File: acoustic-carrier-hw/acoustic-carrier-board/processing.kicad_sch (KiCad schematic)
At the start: 22 parts, among them IC1 ECP5-BGA256, J2 Conn_01x04_Socket, J4 Conn_01x06_Socket, U4 W25Q128JVS

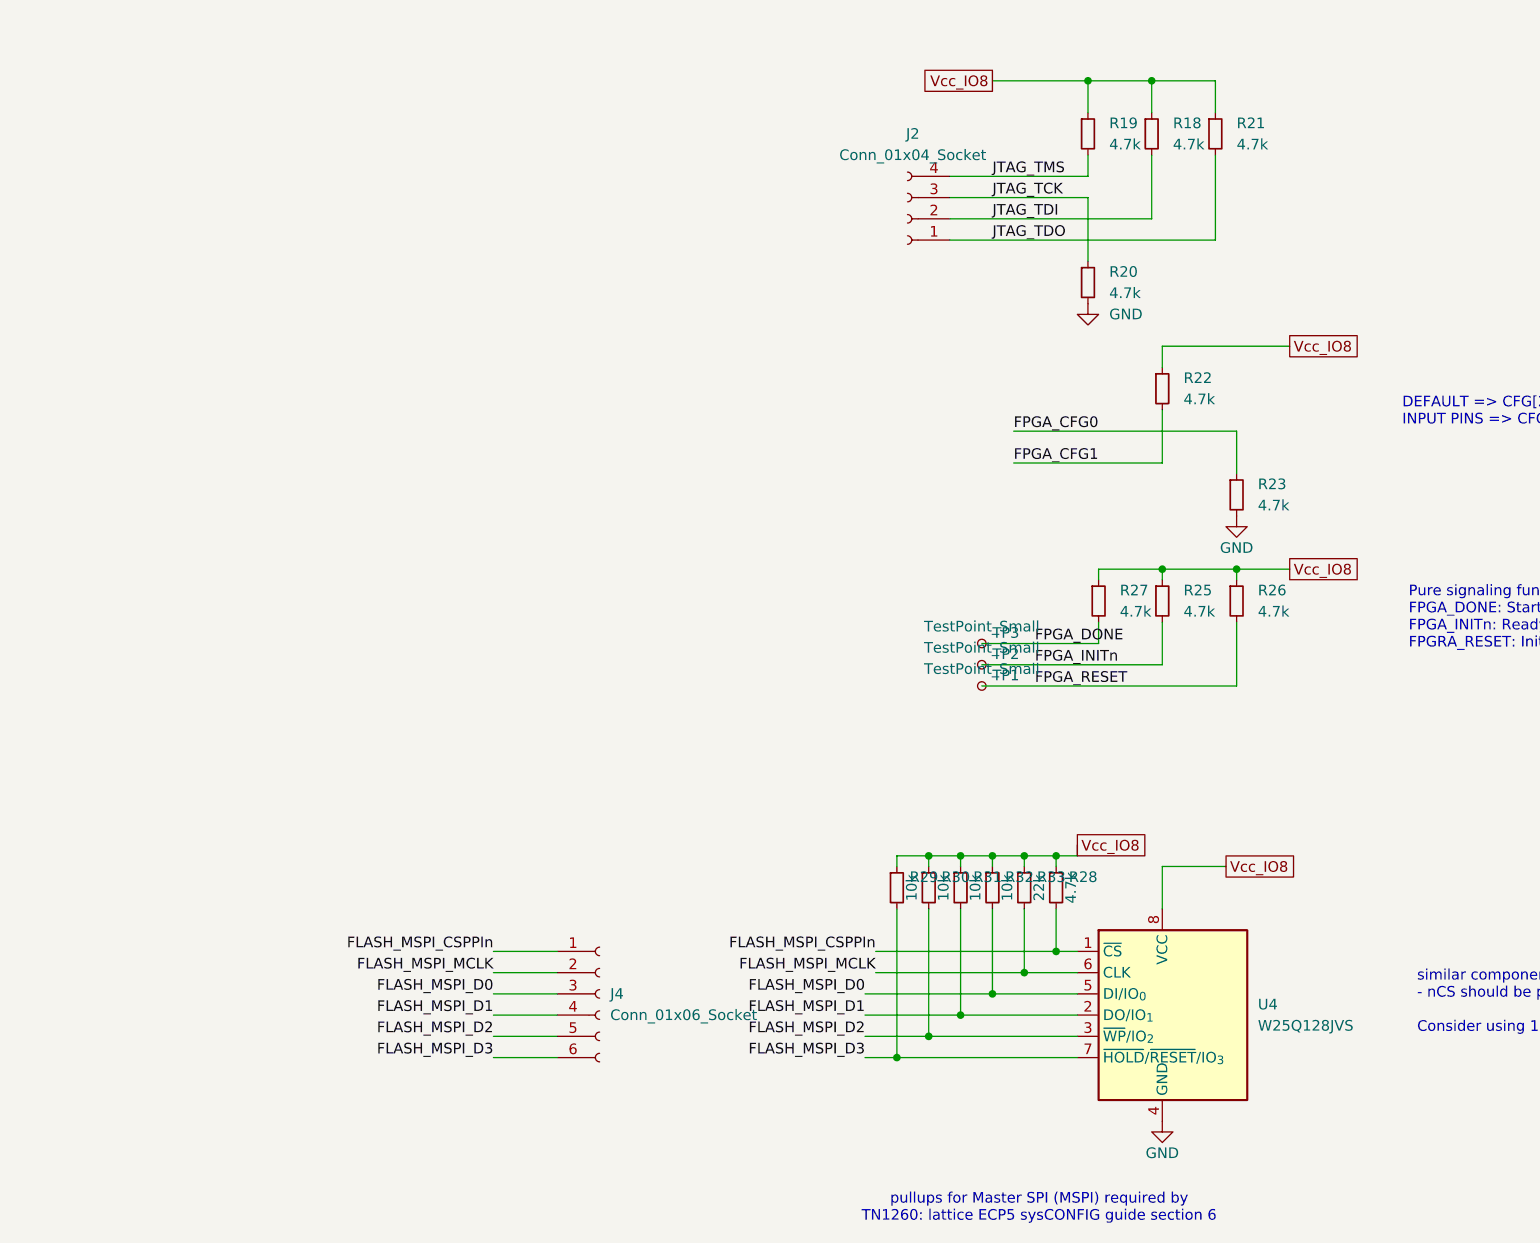
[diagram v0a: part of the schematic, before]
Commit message: [acoustic-carrier-board] Added ethernet PHY
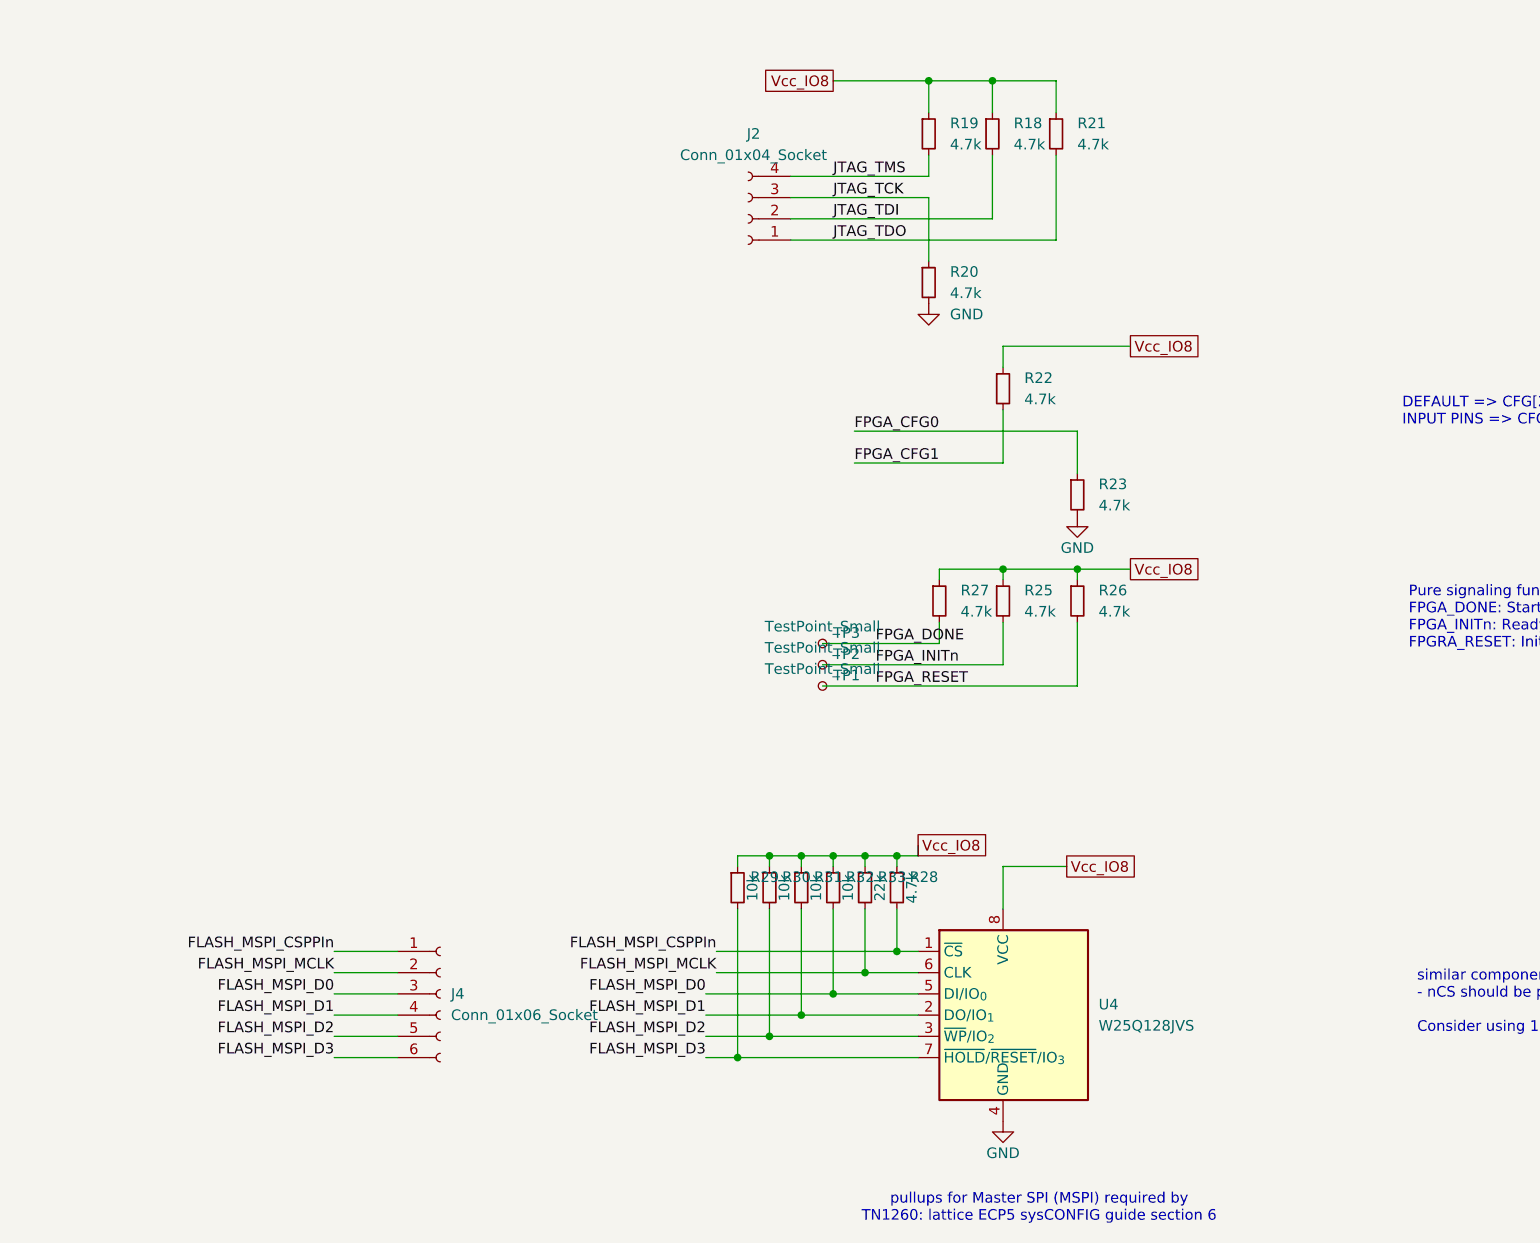
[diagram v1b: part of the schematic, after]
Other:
- moved on the sheet: J2, J4, R18, R19, R20, R21, R22, R23, R25, R26, R27, R28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

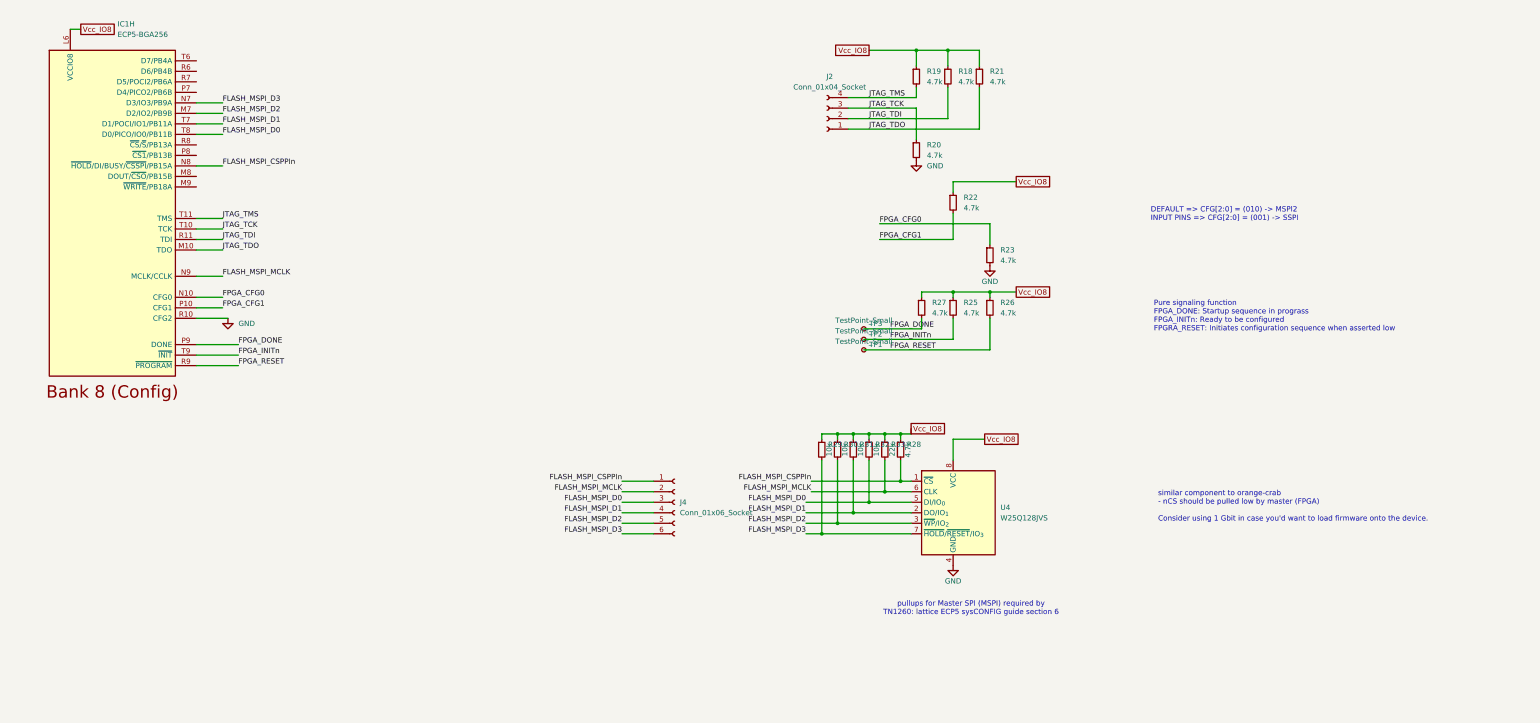
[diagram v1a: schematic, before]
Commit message: [carrier] Added decoupling for DDR (next) Finish power supply
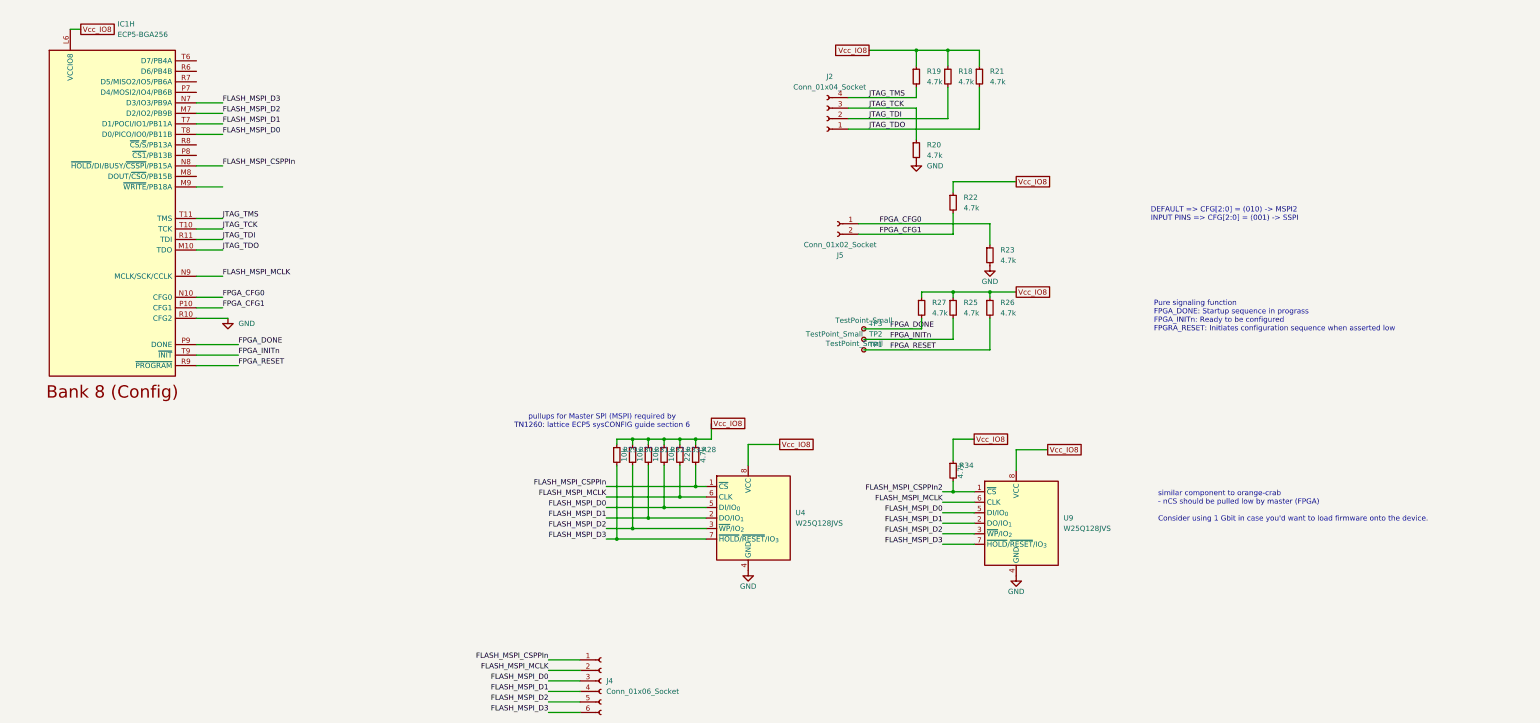
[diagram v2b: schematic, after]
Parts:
- added J5: Conn_01x02_Socket, symbol Connector:Conn_01x02_Socket
- added R34: 4.7k, Resistor_SMD:R_0402_1005Metric, symbol Device:R_Small
- added U9: W25Q128JVS, Package_SO:SOIC-8_5.3x5.3mm_P1.27mm, symbol Memory_Flash:W25Q128JVS
- U4: LCSC Part Number (none) -> C113767; Manufacturing Part Number (none) -> W25Q128JVSIQ
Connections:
- net FLASH_MSPI_D0: now also U9.5 (DI/IO_{0})
- net FLASH_MSPI_D1: now also U9.2 (DO/IO_{1})
- net FLASH_MSPI_D2: now also U9.3 (~{WP}/IO_{2})
- net FLASH_MSPI_D3: now also U9.7 (~{HOLD}/~{RESET}/IO_{3})
- net FLASH_MSPI_MCLK: now also U9.6 (CLK)
- net FPGA_CFG0: now also J5.1 (Pin_1)
- net FPGA_CFG1: now also J5.2 (Pin_2)
- net GND: now also U9.4 (GND)
- net Vcc_IO8: now also R34.1, U9.8 (VCC)
- new net FLASH_MSPI_CSPPIn2: R34.2, U9.1 (~{CS})
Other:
- moved on the sheet: J4, R28, R29, R30, R31, R32, R33, U4

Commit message: added decoupling and power flags
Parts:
- IC1: footprint BGA256C80P16X16_1400X1400X170 -> (none)
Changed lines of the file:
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@@
 			)
 		)
-		(property "Footprint" "BGA256C80P16X16_1400X1400X170"
+		(property "Footprint" ""
 			(at -44.45 -21.59 0)
 			(effects

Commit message: [carrier] Added decoupling to ethernet PHY
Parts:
- IC1: footprint (none) -> BGA256C80P16X16_1400X1400X170
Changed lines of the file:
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@@
 			)
 		)
-		(property "Footprint" ""
+		(property "Footprint" "BGA256C80P16X16_1400X1400X170"
 			(at -44.45 -21.59 0)
 			(effects

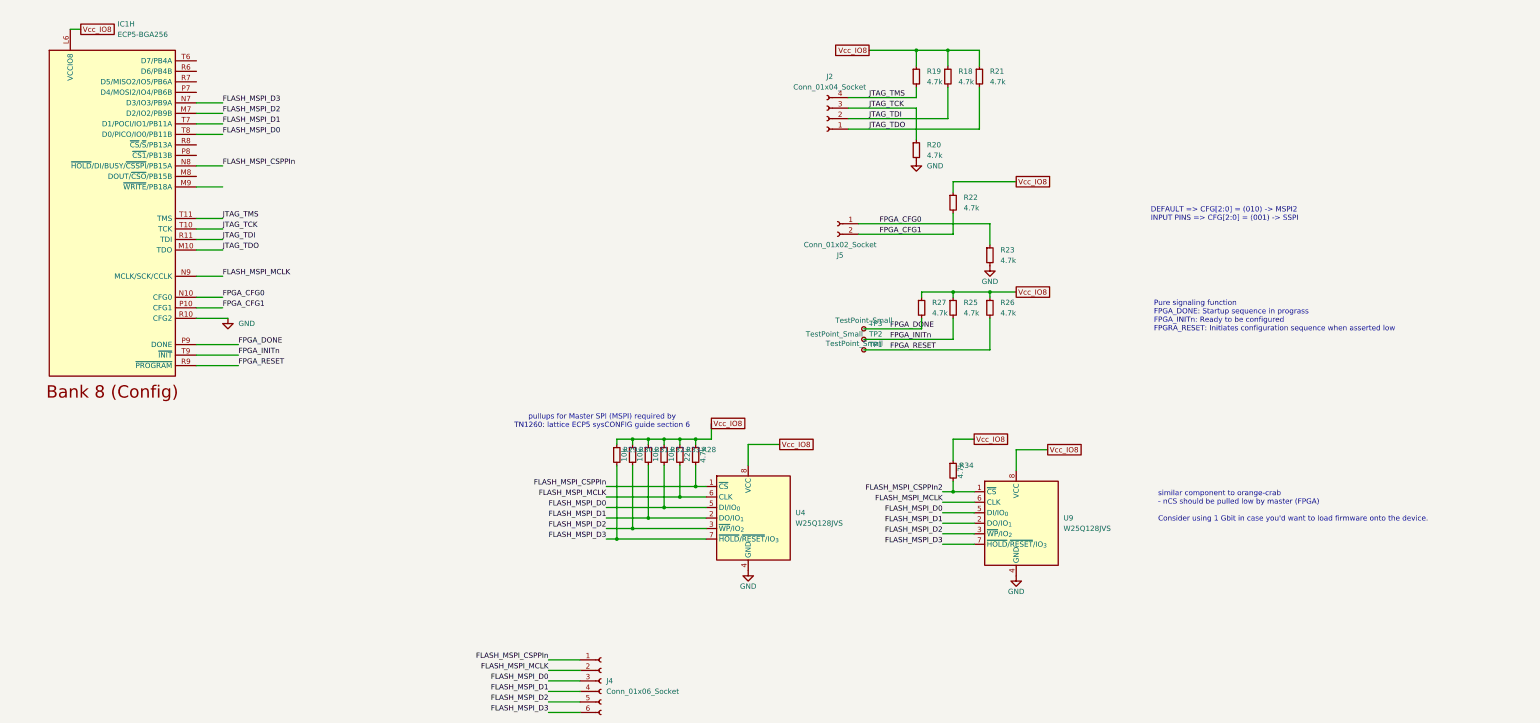
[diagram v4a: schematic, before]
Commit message: [carrier] Reorganized carrier board schematic, added lcsc part numbers (next) check schematic before component placement
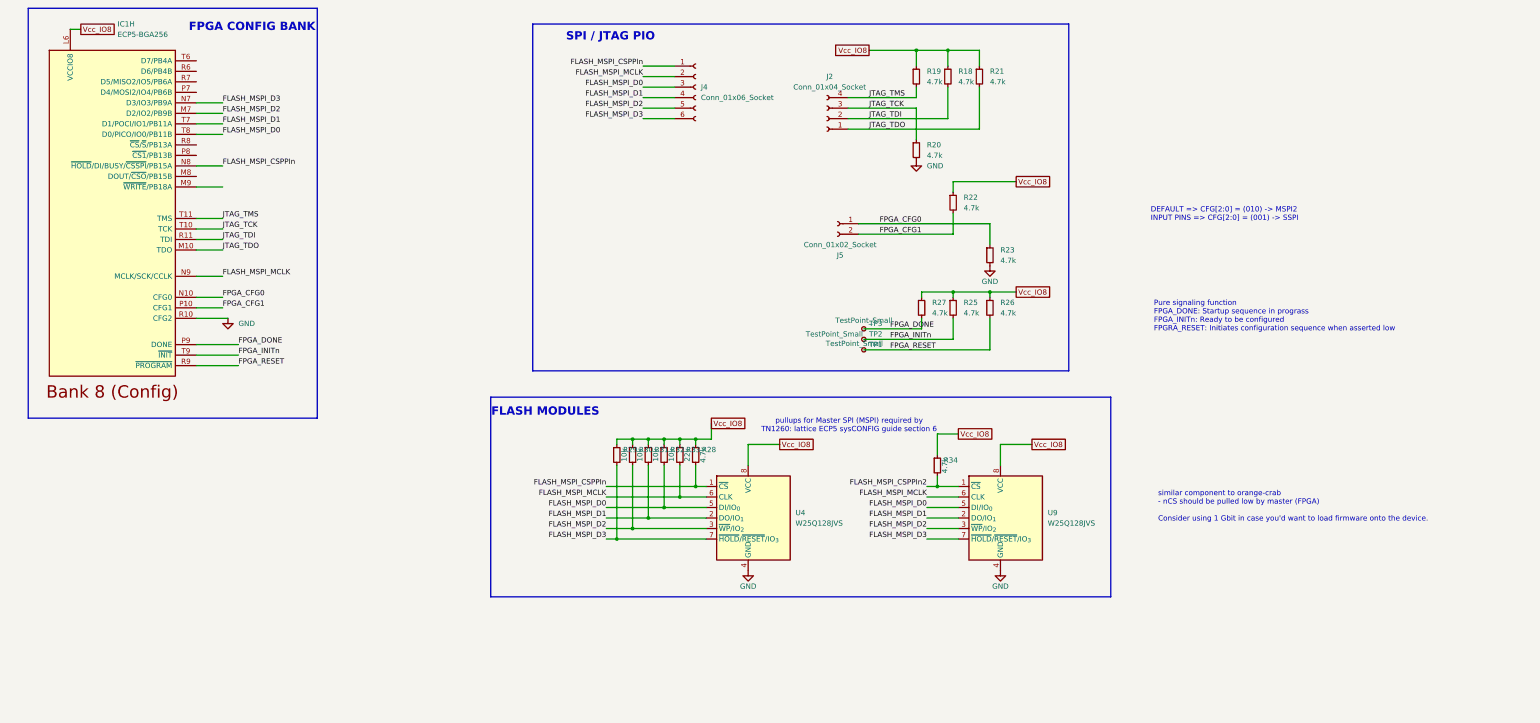
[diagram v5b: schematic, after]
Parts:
- R18, R19, R20, R21, R22, R23, R25, R26, R27, R28, R34: LCSC Part Number C25900 -> (none); LPN (none) -> 0402WGF4701TCE; MPN (none) -> C25900; Manufacturing Part Number 0402WGF4701TCE -> (none)
- R29, R30, R31, R32: LCSC Part Number C25744 -> (none); LPN (none) -> 0402WGF1002TCE; MPN (none) -> C25744; Manufacturing Part Number 0402WGF1002TCE -> (none)
- R33: LCSC Part Number C25768 -> (none); LPN (none) -> C25768; MPN (none) -> 0402WGF2202TCE; Manufacturing Part Number 0402WGF2202TCE -> (none)
- U4, U9: LCSC Part Number C113767 -> (none); LPN (none) -> C113767; MPN (none) -> W25Q128JVSIQ; Manufacturing Part Number W25Q128JVSIQ -> (none)
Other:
- note added: "FLASH MODULES"
- note added: "FPGA CONFIG BANK"
- note added: "SPI / JTAG PIO"
- moved on the sheet: J4, R34, U9

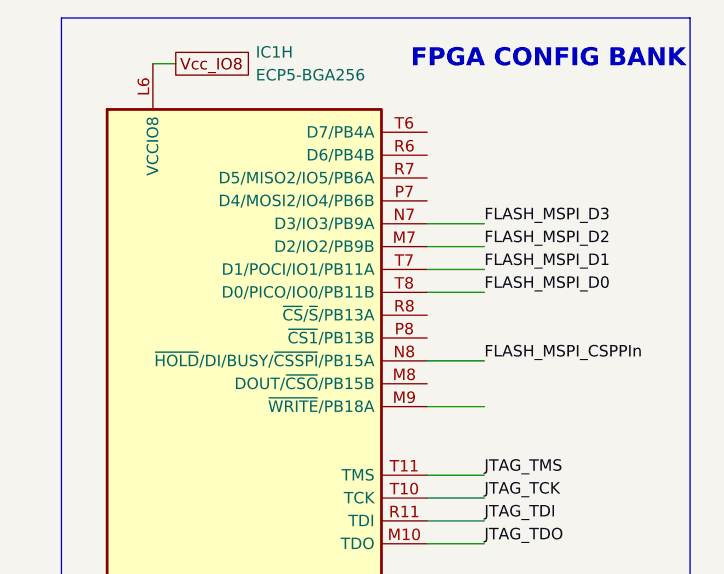
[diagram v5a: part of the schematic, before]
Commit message: [carrier] Started schematic check, replaced 8 with 16 pin connectors
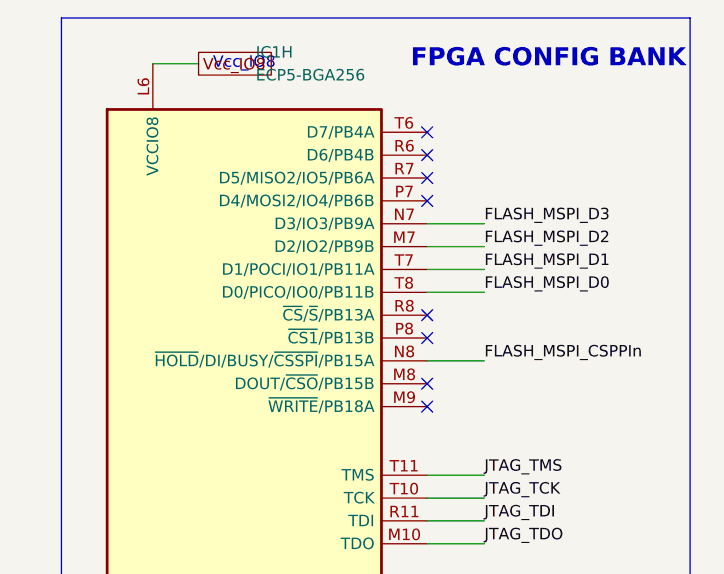
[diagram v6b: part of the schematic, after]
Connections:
- no-connect marks 0 -> 8
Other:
- note added: "Vcc_IO8"
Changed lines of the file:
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@@
+		)
+	)
+	(text "Vcc_IO8"
+		(exclude_from_sim no)
+		(at 36.83 21.59 0)
+		(effects
+			(font
+				(size 1.27 1.27)
+			)
 		)
 	)
@@
 		(color 0 0 0 0)
 	)
+	(no_connect
+		(at 57.15 59.69)
+	)
+	(no_connect
+		(at 57.15 49.53)
+	)
+	(no_connect
+		(at 57.15 36.83)
+	)
+	(no_connect
+		(at 57.15 29.21)
+	)
+	(no_connect
+		(at 57.15 52.07)
+	)
+	(no_connect
+		(at 57.15 57.15)
+	)
+	(no_connect
+		(at 57.15 34.29)
+	)
+	(no_connect
+		(at 57.15 31.75)
+	)
 	(wire
 		(pts
@@
 	(wire
 		(pts
-			(xy 29.21 21.59) (xy 26.67 21.59)
+			(xy 26.67 21.59) (xy 31.75 21.59)
 		)
 		(stroke
@@
 		(pts
 			(xy 165.1 38.1) (xy 172.72 38.1)
-		)
-		(stroke
-			(width 0)
-			(type default)
-		)
-	)
-	(wire
-		(pts
-			(xy 57.15 59.69) (xy 63.5 59.69)
 		)
 		(stroke
@@
 	(global_label "Vcc_IO8"
 		(shape passive)
-		(at 29.21 21.59 0)
+		(at 31.75 21.59 0)
 		(fields_autoplaced yes)
 		(effects
@@
 		)
 		(property "Intersheetrefs" "${INTERSHEET_REFS}"
-			(at 38.4621 21.59 0)
+			(at 41.0021 21.59 0)
 			(effects
 				(font
